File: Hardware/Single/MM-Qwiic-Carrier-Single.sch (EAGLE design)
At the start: 52 parts, among them J15 MICROMOD-2222-C, J2 QWIIC_RIGHT_ANGLE, J5 Vertical Qwiic Connector, U1 MCP73831, U5 AP7361C-33FGEUDFN-8

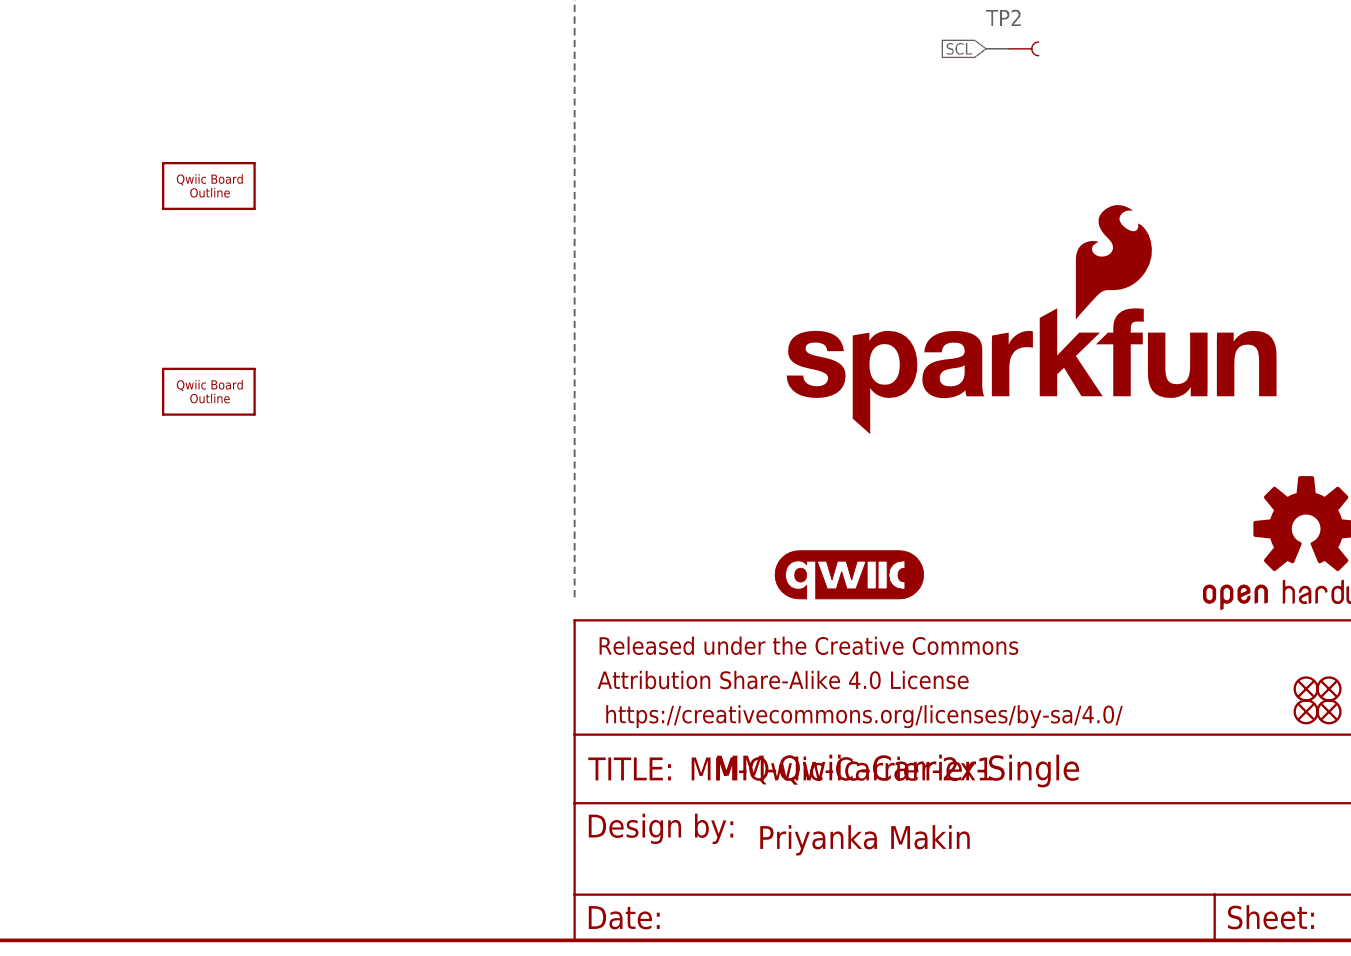
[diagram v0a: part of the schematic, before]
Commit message: Move SF logo, board name silk screen on bottom
Renamed eagle files from 1x1, 2x1 to single, double
Cleaned up library files
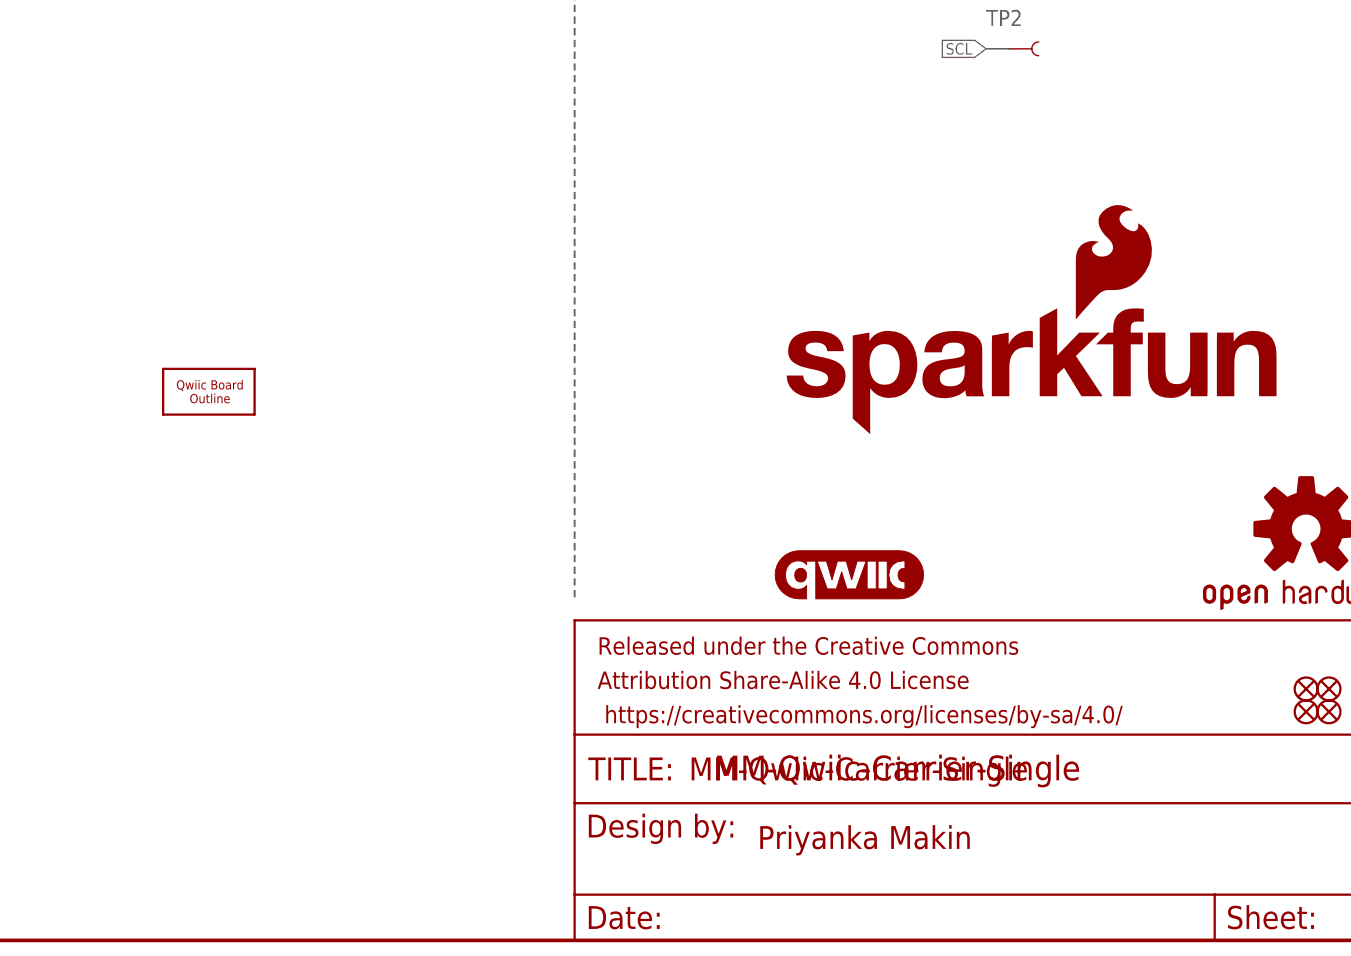
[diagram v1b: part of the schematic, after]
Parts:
- removed U$2: QWIIC_BOARD_OUTLINESTANDOFF, SparkFun-Boards:QWIIC_BOARD_OUTLINESTANDOFF
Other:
- note added: "MM-Qwiic-Carrier-Single"
- note removed: "MM-Qwiic-Carrier-2x1"
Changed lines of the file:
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@@
 <?xml version="1.0" encoding="utf-8"?>
 <!DOCTYPE eagle SYSTEM "eagle.dtd">
-<eagle version="9.6.2">
+<eagle version="9.5.2">
 <drawing>
 <settings>
@@
 <part name="J6" library="SparkFun-Connectors" deviceset="CONN_09" device="NO_SILK"/>
 <part name="SUPPLY17" library="SparkFun-PowerSymbols" deviceset="3.3V" device=""/>
-<part name="U$2" library="SparkFun-Boards" deviceset="QWIIC_BOARD_OUTLINE" device="STANDOFF"/>
 </parts>
 <sheets>
@@
 <text x="58.674" y="263.906" size="2.54" layer="94" font="vector" align="center">Universal MicroMod Connector</text>
 <text x="350.52" y="10.16" size="2.54" layer="94" font="vector">Priyanka Makin</text>
-<text x="342.9" y="17.78" size="2.54" layer="94" font="vector">MM-Qwiic-Carrier-2x1</text>
+<text x="342.9" y="17.78" size="2.54" layer="94" font="vector">MM-Qwiic-Carrier-Single</text>
 <text x="142.24" y="238.76" size="2.54" layer="94" font="vector" align="center">LED</text>
 <text x="419.1" y="7.62" size="2.54" layer="94" font="vector">v10</text>
@@
 <attribute name="VALUE" x="208.28" y="38.354" size="1.778" layer="96" align="bottom-center"/>
 </instance>
-<instance part="U$2" gate="G$1" x="289.56" y="83.82" smashed="yes"/>
 </instances>
 <busses>
